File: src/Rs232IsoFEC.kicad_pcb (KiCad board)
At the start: 2 copper layers, 24 x 27.9 mm, 25 parts, among them J1 B3B-XH-A, P1 105444-0001, Q1 DMP3099L-13, U1 FT232RL, U2 ADM3251E

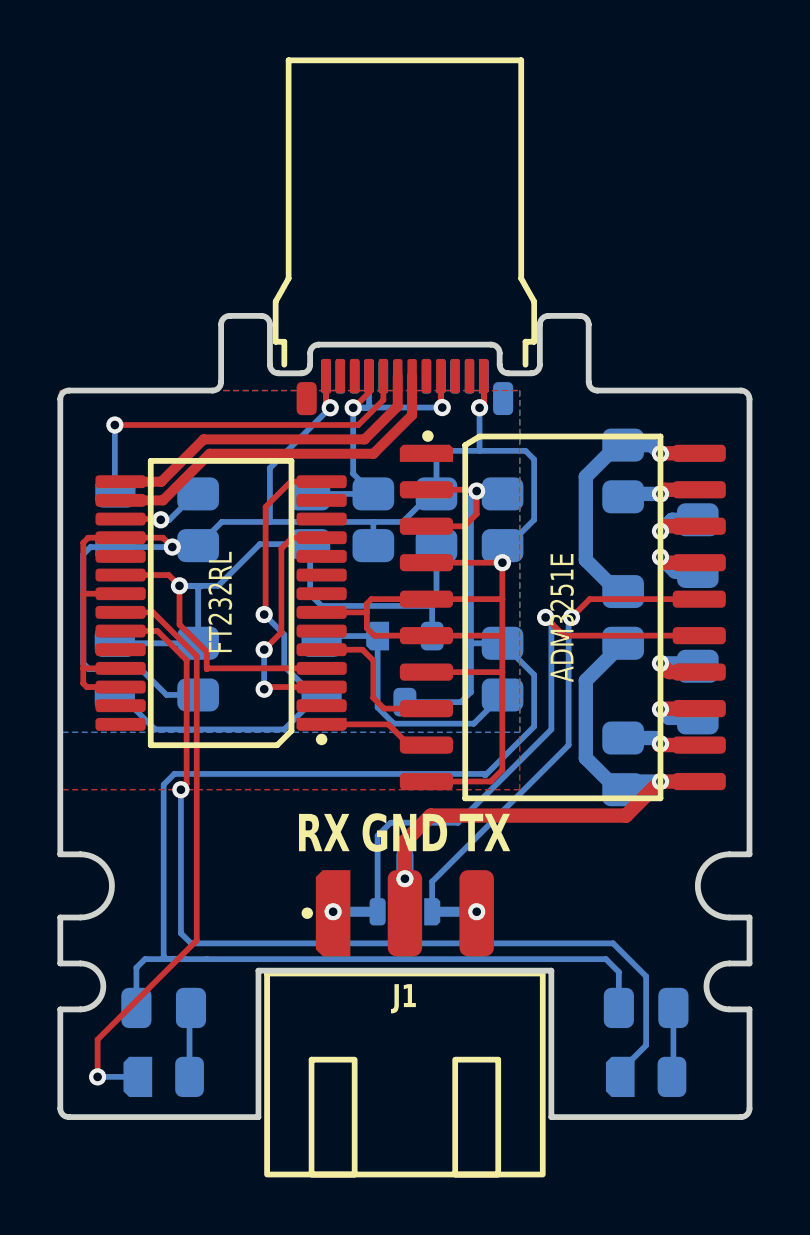
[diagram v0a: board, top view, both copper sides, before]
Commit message: Changed conntector to 5-pin variant
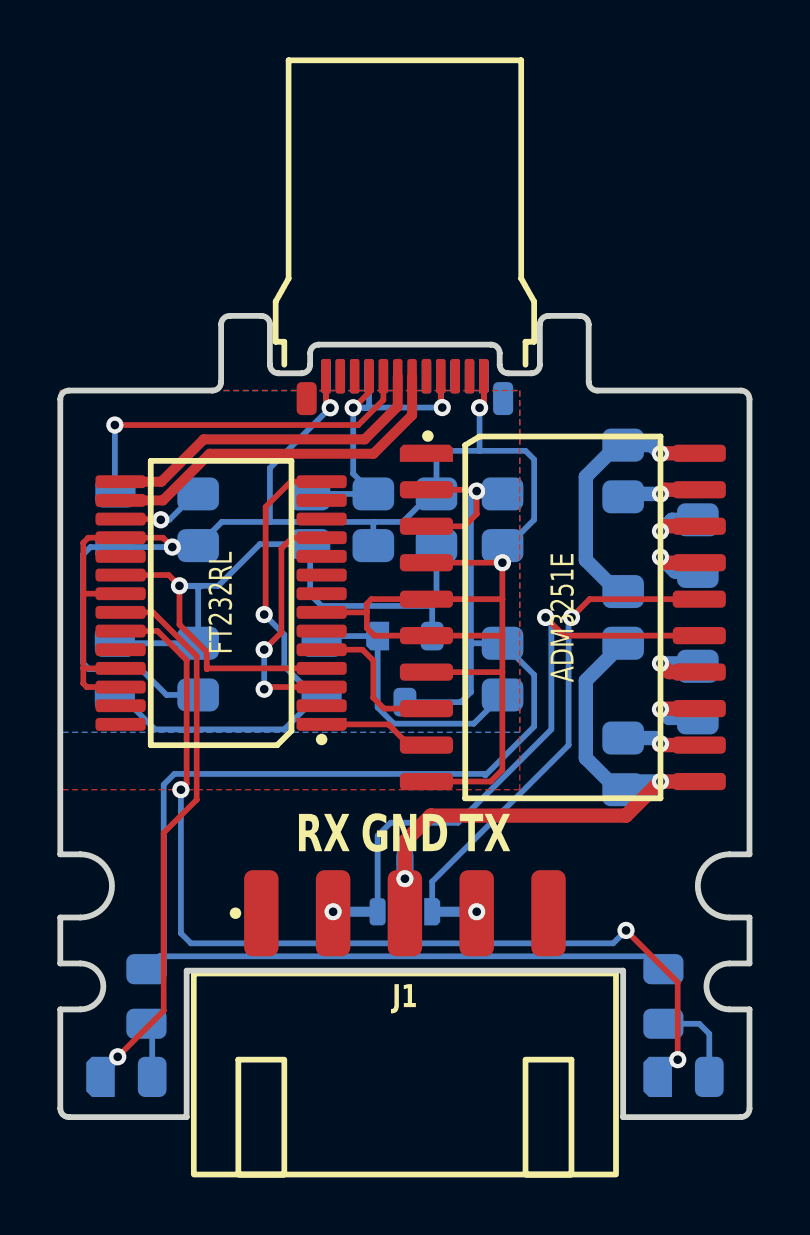
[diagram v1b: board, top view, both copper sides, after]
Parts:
- J1: value B3B-XH-A -> B5B-XH-A; footprint Medo64:J JST XH Edge [UART] (3w) -> Medo64:J JST XH Edge [UART] (5w)
- moved DS2 1.30 mm to (41.7, 46.5)
- moved DS1 1.30 mm to (22.3, 46.5)
- moved R1 0.72 mm to (23.0, 43.7), turned to -90 degrees
- moved R2 0.72 mm to (41.0, 43.7), turned to -90 degrees
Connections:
- J1 pad 1: ISO_RXD -> (no net)
- J1 pad 2: ISO_GND -> ISO_RXD
- J1 pad 3: ISO_TXD -> ISO_GND
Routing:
- net 5V_SW: track 59.6 -> 57.6 mm
- net LED_TXD: track 32.8 -> 34.3 mm, vias 1 -> 3
- net LED_RXD: track 20.8 -> 19.3 mm
- net LED_TXD': track 2.35 -> 3.24 mm
- net LED_RXD': track 2.35 -> 1.65 mm
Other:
- outline, holes or cut-outs redrawn

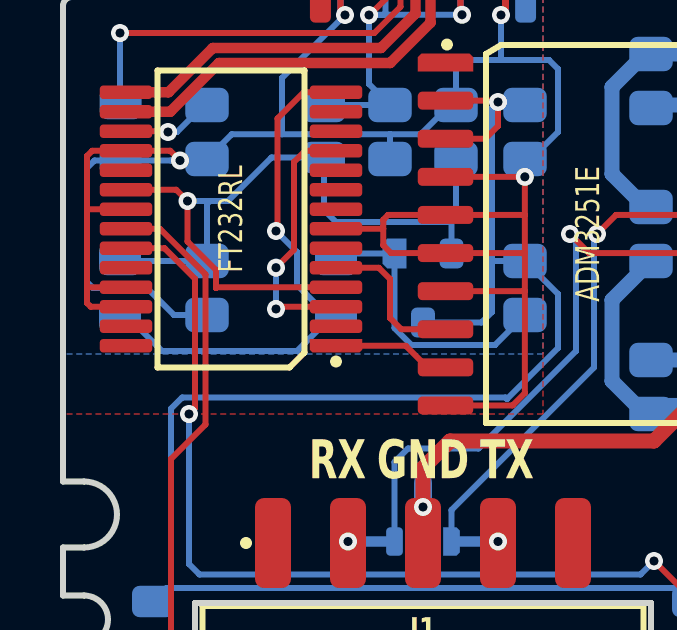
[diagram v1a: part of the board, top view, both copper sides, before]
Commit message: Refactoring copper pour
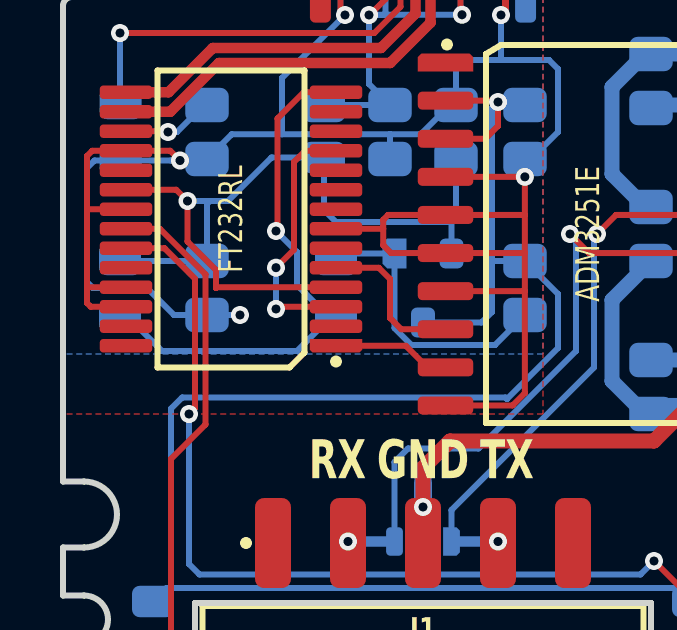
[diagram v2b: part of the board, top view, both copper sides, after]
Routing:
- net GND: track 83.4 -> 84.5 mm, vias 4 -> 5
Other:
- rule pad_to_mask_clearance: 0 -> 0.05
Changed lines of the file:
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@@
       (dielectric_constraints no)
     )
-    (pad_to_mask_clearance 0)
+    (pad_to_mask_clearance 0.05)
     (aux_axis_origin 20 20)
     (pcbplotparams
@@
         (effects (font (size 0.8 0.6) (thickness 0.15)) (justify mirror))
     )
+    (fp_text user "D" (at 0 0.5) (layer "Cmts.User" knockout)
+        (effects (font (size 0.13 0.07) (thickness 0.01) bold))
+    )
+    (fp_text user "G" (at -0.95 -0.5) (layer "Cmts.User" knockout)
+        (effects (font (size 0.13 0.07) (thickness 0.01) bold))
+    )
     (fp_text user "S" (at 0.95 -0.5) (layer "Cmts.User" knockout)
         (effects (font (size 0.13 0.07) (thickness 0.01) bold))
     )
-    (fp_text user "G" (at -0.95 -0.5) (layer "Cmts.User" knockout)
-        (effects (font (size 0.13 0.07) (thickness 0.01) bold))
-    )
-    (fp_text user "D" (at 0 0.5) (layer "Cmts.User" knockout)
-        (effects (font (size 0.13 0.07) (thickness 0.01) bold))
-    )
     (fp_rect (start -1.35 0.25) (end 1.35 -0.25)
       (stroke (width 0.2) (type default)) (fill none) (layer "B.SilkS"))
-    (fp_circle (center -1.575 -1.15) (end -1.425 -1.15)
+    (fp_circle (center -1.65 -1.15) (end -1.5 -1.15)
       (stroke (width 0.1) (type solid)) (fill solid) (layer "B.SilkS"))
     (fp_rect (start -1.75 1.95) (end 1.75 -1.95)
@@
   (via (at 29.4 23.2) (size 0.6) (drill 0.3) (layers "F.Cu" "B.Cu") (net 7))
   (via (at 34.6 23.2) (size 0.6) (drill 0.3) (layers "F.Cu" "B.Cu") (net 7))
+  (via (at 25.9 33.2) (size 0.6) (drill 0.3) (layers "F.Cu" "B.Cu") (net 7))
   (segment (start 21.05 28.05) (end 21.92 28.05) (width 0.2) (layer "B.Cu") (net 7))
   (segment (start 29.4 23.2) (end 27.3 25.3) (width 0.2) (layer "B.Cu") (net 7))
@@
   (segment (start 25.625 27.175) (end 27.3 27.175) (width 0.2) (layer "B.Cu") (net 7))
   (segment (start 36.5 25) (end 36.2 24.7) (width 0.2) (layer "B.Cu") (net 7))
+  (segment (start 25.9 33.2) (end 24.8 33.2) (width 0.2) (layer "B.Cu") (net 7))
   (segment (start 31.925 27.175) (end 32.9 26.2) (width 0.2) (layer "B.Cu") (net 7))
   (segment (start 35.4 28.59) (end 35.395 28.595) (width 0.2) (layer "B.Cu") (net 7))
@@
   (segment (start 27.1 33) (end 27.1 31.622198) (width 0.2) (layer "B.Cu") (net 27))
   (zone (net 7) (net_name "GND") (layer "F.Cu") (hatch edge 0.5)
-    (connect_pads (clearance 0.35))
-    (min_thickness 0.25) (filled_areas_thickness no)
+    (connect_pads no (clearance 0.3))
+    (min_thickness 0.3) (filled_areas_thickness no)
     (fill yes (thermal_gap 0.5) (thermal_bridge_width 0.5))
     (polygon
@@
   )
   (zone (net 7) (net_name "GND") (layer "B.Cu") (hatch edge 0.5)
-    (connect_pads (clearance 0.35))
-    (min_thickness 0.25) (filled_areas_thickness no)
+    (connect_pads no (clearance 0.3))
+    (min_thickness 0.3) (filled_areas_thickness no)
     (fill yes (thermal_gap 0.5) (thermal_bridge_width 0.5))
     (polygon
